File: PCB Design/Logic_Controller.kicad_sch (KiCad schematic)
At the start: 30 parts, among them J31 Conn_01x15, J32 Conn_01x15, J33 UART0, J34 UART2, J35 GPIO, J36 Display, J37 I2C, J38 I2C, J39 SPI, J40 GPIO, SW31 EN, SW32 BOOT, U31 AMS1117-3.3, U32 ESP32-WROOM-32UE, U33 TCA9406DC

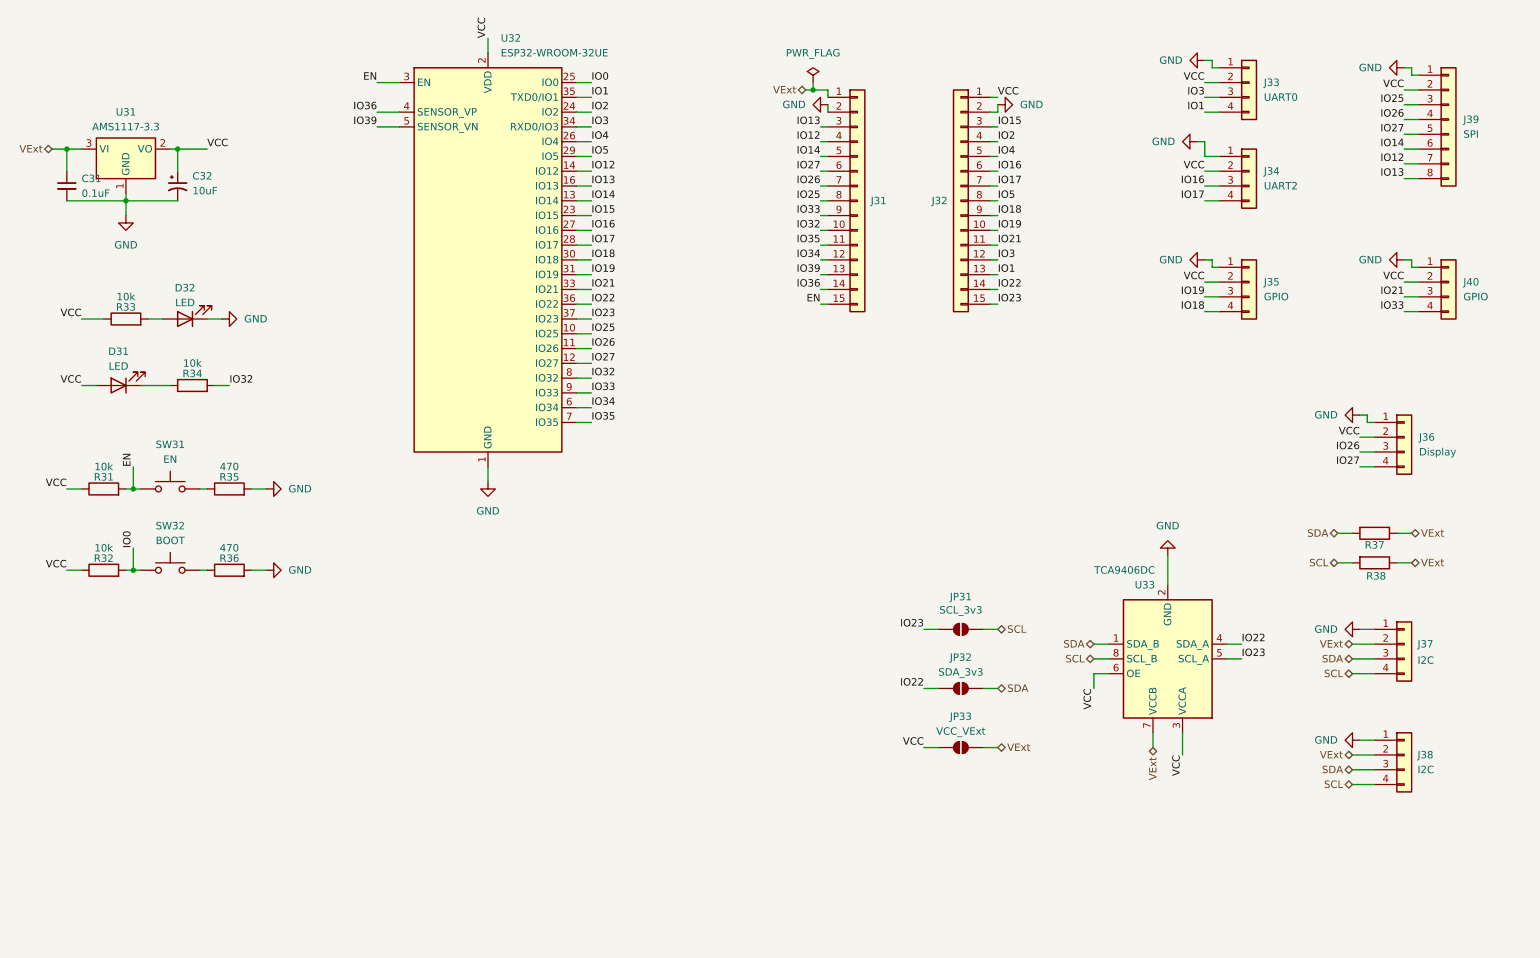
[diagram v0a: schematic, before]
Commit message: Panelize
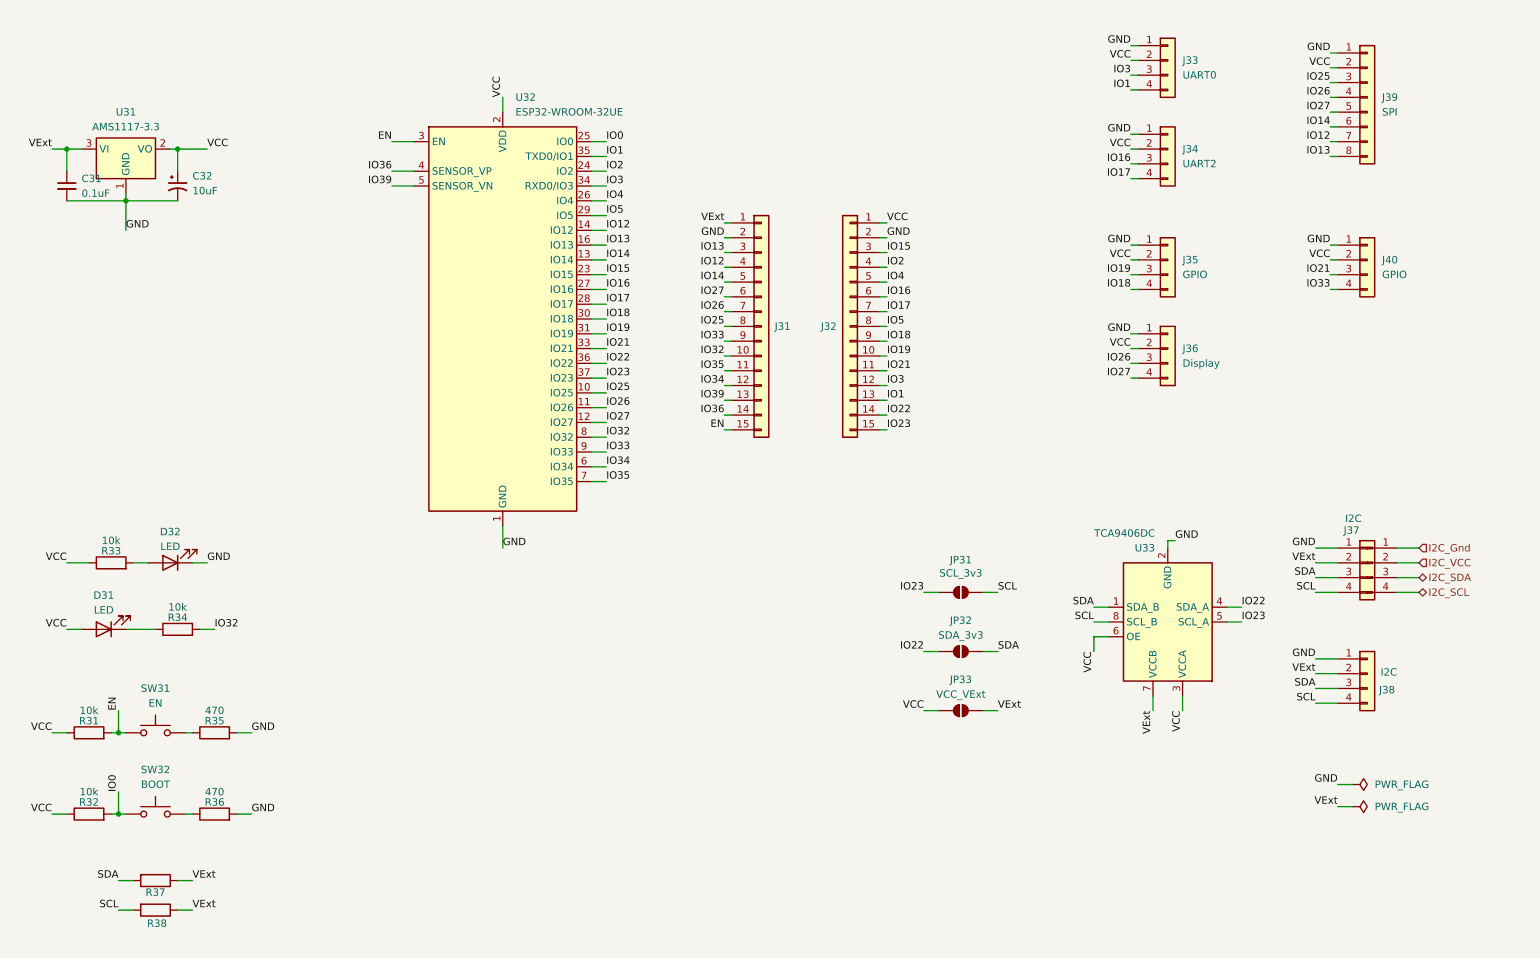
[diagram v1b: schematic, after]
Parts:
- added J44: Conn_01x04_Pin, symbol Connector:Conn_01x04_Pin
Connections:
- new net I2C_Gnd: J44.1 (Pin_1)
- new net I2C_SCL: J44.4 (Pin_4)
- new net I2C_SDA: J44.3 (Pin_3)
- new net I2C_VCC: J44.2 (Pin_2)
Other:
- moved on the sheet: D31, D32, J31, J32, J33, J34, J35, J36, J37, J38, J39, J40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

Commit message: Added Multiplexer
Added separate IO Multiplexer breakout
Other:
- title: I2C Relay Controler -> Logic Controller
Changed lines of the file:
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@@
 	(paper "A4")
 	(title_block
-		(title "I2C Relay Controler")
+		(title "Logic Controller")
 		(date "2024-03-19")
 		(rev "2")

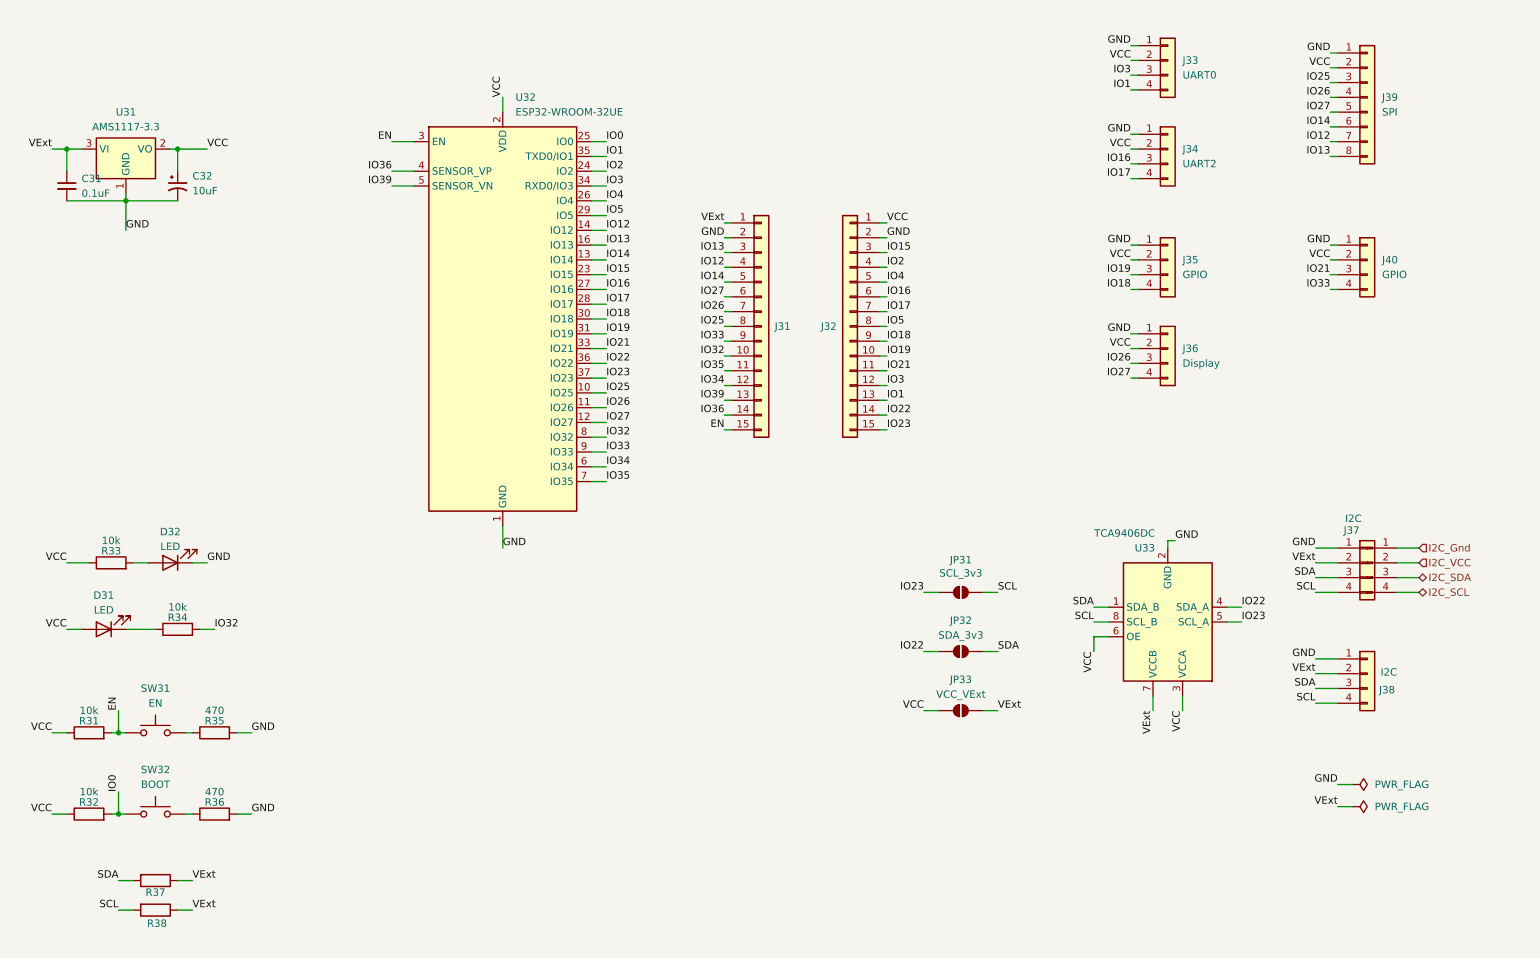
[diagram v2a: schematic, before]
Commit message: Tweaks and Updates
Added OSCIO pin to breakout board.
A few more tweaks
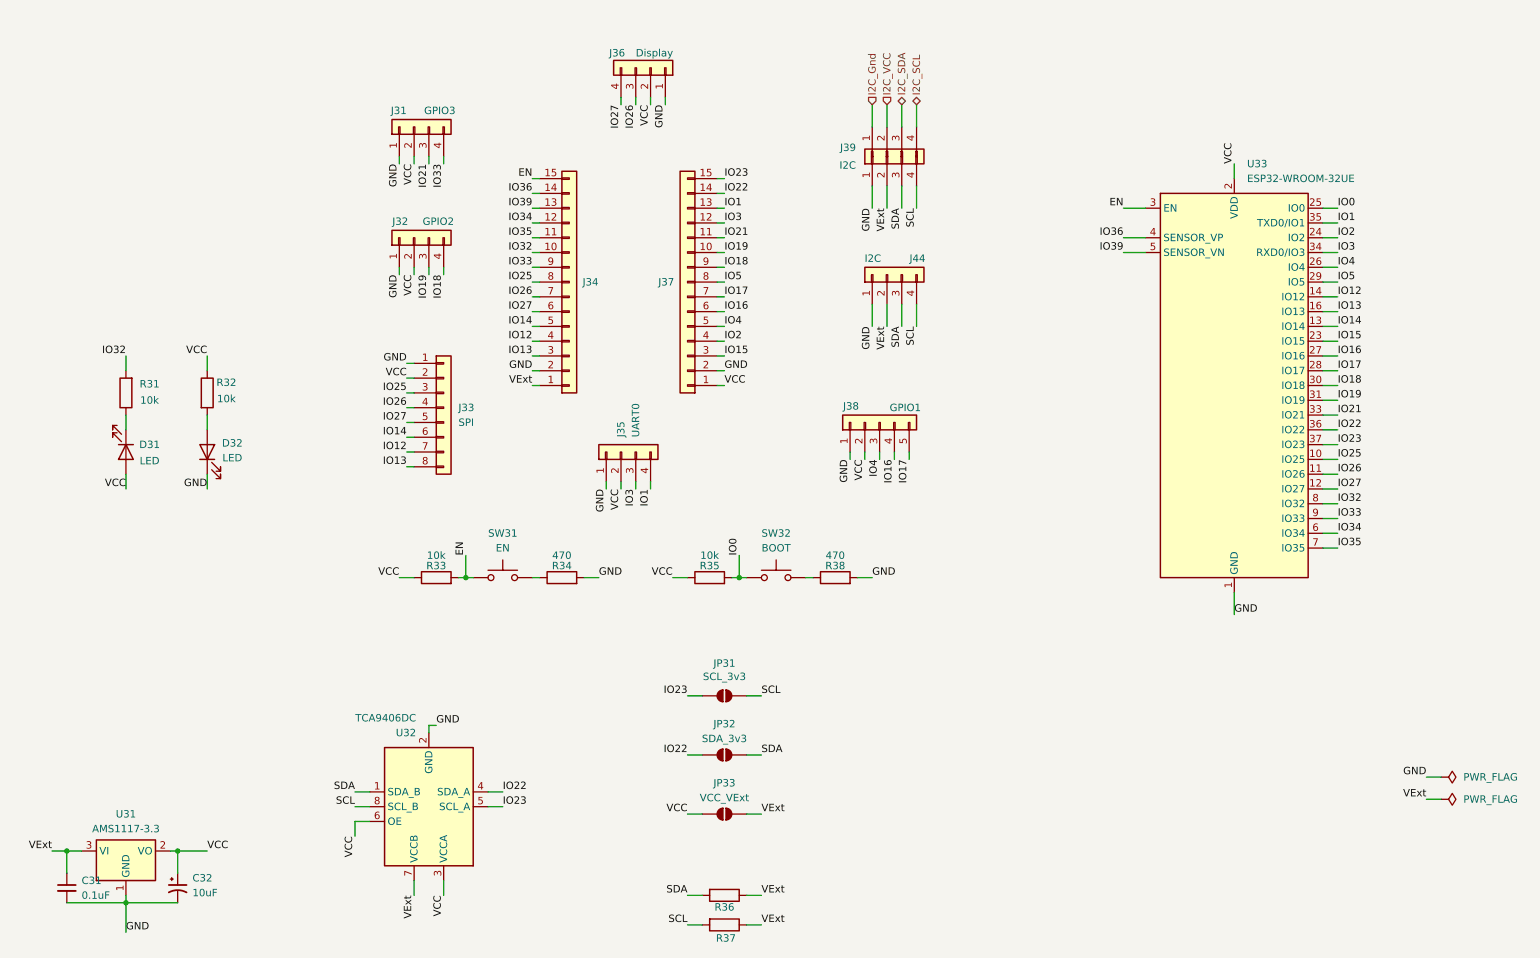
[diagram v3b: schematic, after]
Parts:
- J31: renamed from J40; value GPIO -> GPIO3
- J32: renamed from J35; value GPIO -> GPIO2
- J38: renamed from J34; value UART2 -> GPIO1; footprint Connector_JST:JST_XH_B4B-XH-A_1x04_P2.50mm_Vertical -> Connector_JST:JST_XH_B5B-XH-A_1x05_P2.50mm_Vertical; symbol Connector_Generic:Conn_01x04 -> Connector_Generic:Conn_01x05
- renumbered J39 to J33, J31 to J34, J33 to J35, J32 to J37, J37 to J39, J44 to J40, J38 to J44, R34 to R31, R33 to R32, R31 to R33, R35 to R34, R32 to R35, R37 to R36, R38 to R37, R36 to R38, U33 to U32, U32 to U33
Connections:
- net IO16: now also J38.4 (Pin_4); no longer J38.3 (Pin_3)
- net IO17: now also J38.5 (Pin_5); no longer J38.4 (Pin_4)
- net IO4: now also J38.3 (Pin_3)
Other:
- moved on the sheet: C31, C32, D31, D32, J31, J32, J33, J34, J35, J36, J37, J39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

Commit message: Testpoints to schematic.
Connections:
- net GND: now also D31.1 (K)
- net VCC: no longer D31.2 (A)
- net at R31.1: now also D31.2 (A); no longer D31.1 (K)
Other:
- moved on the sheet: D31
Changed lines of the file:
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@@
 	(wire
 		(pts
+			(xy 40.64 93.98) (xy 40.64 96.52)
+		)
+		(stroke
+			(width 0)
+			(type default)
+		)
+	)
+	(wire
+		(pts
 			(xy 87.63 50.8) (xy 87.63 49.53)
 		)
@@
 	(wire
 		(pts
+			(xy 40.64 104.14) (xy 40.64 106.68)
+		)
+		(stroke
+			(width 0)
+			(type default)
+		)
+	)
+	(wire
+		(pts
 			(xy 246.38 63.5) (xy 248.92 63.5)
 		)
@@
 	(wire
 		(pts
-			(xy 40.64 106.68) (xy 40.64 104.14)
-		)
-		(stroke
-			(width 0)
-			(type default)
-		)
-	)
-	(wire
-		(pts
 			(xy 99.06 121.92) (xy 100.33 121.92)
 		)
@@
 	(wire
 		(pts
-			(xy 40.64 93.98) (xy 40.64 96.52)
-		)
-		(stroke
-			(width 0)
-			(type default)
-		)
-	)
-	(wire
-		(pts
 			(xy 110.49 83.82) (xy 111.76 83.82)
 		)
@@
 		)
 	)
-	(label "VCC"
-		(at 40.64 106.68 180)
-		(fields_autoplaced yes)
-		(effects
-			(font
-				(size 1.27 1.27)
-			)
-			(justify right bottom)
-		)
-	)
 	(label "GND"
 		(at 168.91 121.92 0)
@@
 		)
 	)
+	(label "GND"
+		(at 40.64 106.68 180)
+		(fields_autoplaced yes)
+		(effects
+			(font
+				(size 1.27 1.27)
+			)
+			(justify right bottom)
+		)
+	)
 	(label "VCC"
 		(at 143.51 88.9 0)
@@
 	(symbol
 		(lib_id "Device:LED")
-		(at 40.64 100.33 270)
+		(at 40.64 100.33 90)
 		(unit 1)
 		(exclude_from_sim no)
@@
 		(dnp no)
 		(property "Reference" "D31"
-			(at 44.704 99.06 90)
+			(at 36.576 101.6 90)
 			(effects
 				(font
@@
 		)
 		(property "Value" "LED"
-			(at 44.704 101.854 90)
+			(at 36.576 98.806 90)
 			(effects
 				(font

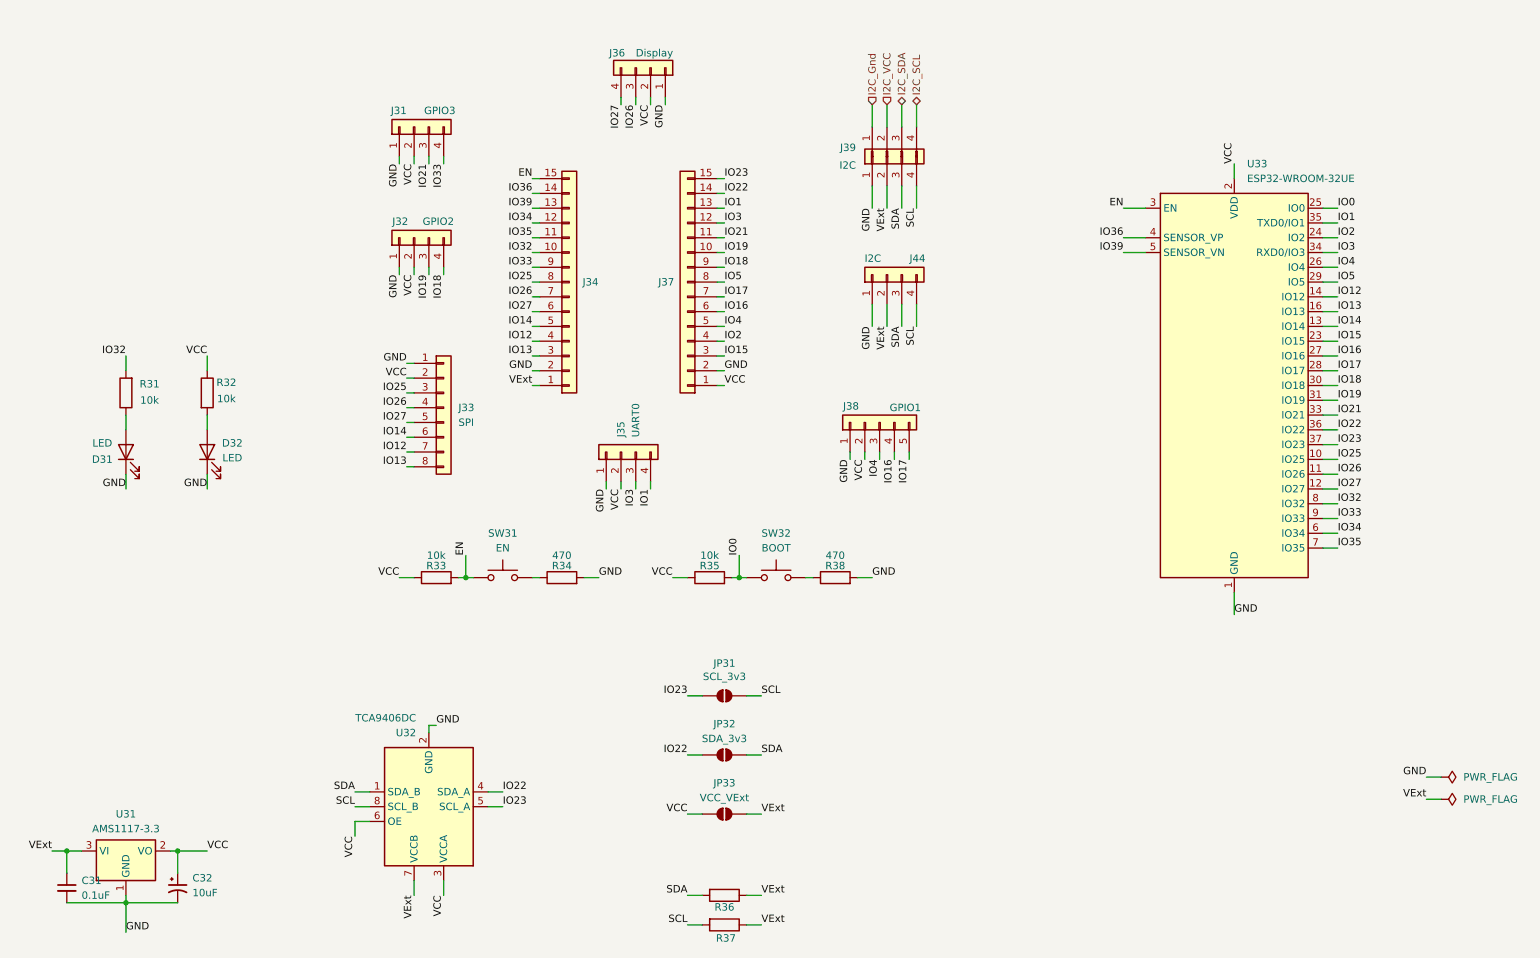
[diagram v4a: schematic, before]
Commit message: Vcc->3v3 Added extra GPIO
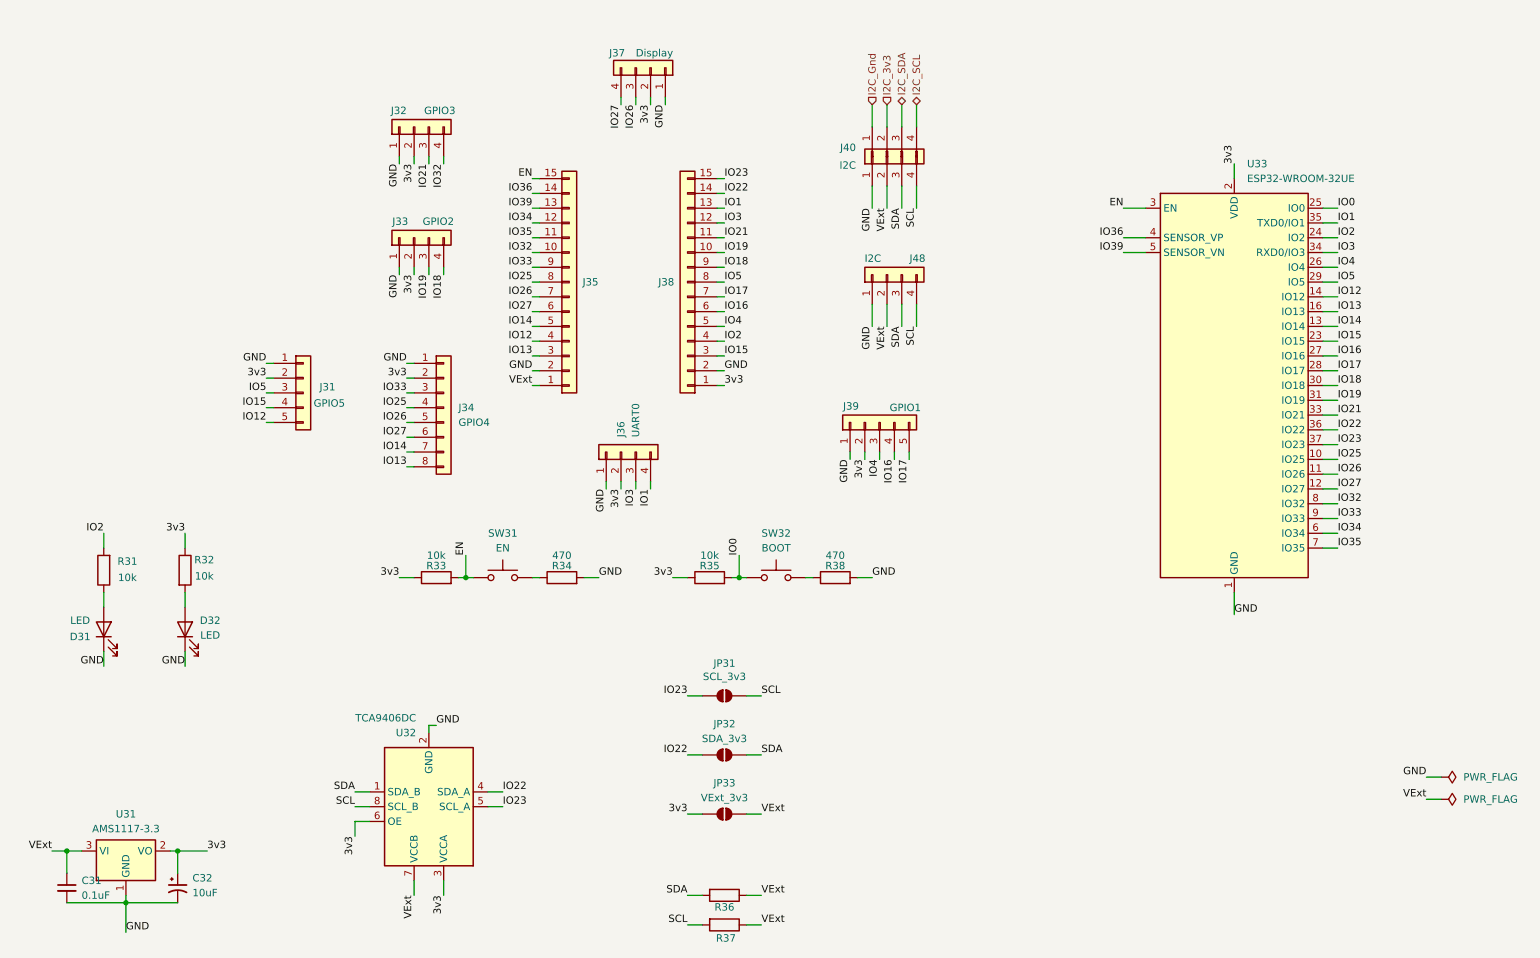
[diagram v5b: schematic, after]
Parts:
- added J31: GPIO5, Connector_JST:JST_XH_B5B-XH-A_1x05_P2.50mm_Vertical, symbol Connector_Generic:Conn_01x05
- J34: renamed from J33; value SPI -> GPIO4
- JP33: value VCC_VExt -> VExt_3v3
- renumbered J31 to J32, J32 to J33, J34 to J35, J35 to J36, J36 to J37, J37 to J38, J38 to J39, J39 to J40, J40 to J44, J44 to J48
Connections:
- net GND: now also J31.1 (Pin_1)
- net IO12: now also J31.5 (Pin_5); no longer J34.7 (Pin_7)
- net IO14: now also J34.7 (Pin_7); no longer J34.6 (Pin_6)
- net IO15: now also J31.4 (Pin_4)
- net IO2: now also R31.2
- net IO25: now also J34.4 (Pin_4); no longer J34.3 (Pin_3)
- net IO26: now also J34.5 (Pin_5); no longer J34.4 (Pin_4)
- net IO27: now also J34.6 (Pin_6); no longer J34.5 (Pin_5)
- net IO32: now also J32.4 (Pin_4); no longer R31.2
- net IO33: now also J34.3 (Pin_3); no longer J32.4 (Pin_4)
- net IO5: now also J31.3 (Pin_3)
- net I2C_VCC renamed I2C_3v3
- net VCC renamed 3v3
- net 3v3: now also J31.2 (Pin_2)
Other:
- moved on the sheet: D31, D32, R31, R32
